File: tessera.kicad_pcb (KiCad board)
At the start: 4 copper layers, 0 parts

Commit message: feat(sch): preliminary Tessera Badge schematic
- Add sheets for LEDs, USB connector, MCU, NFC, power and STSAFE-A120.
- Drop the old placeholder sections.
- Bump the lib submodule and add IPN as a BOM column in the kibot
  outputs to reflect the DB-library parts now placed in the schematic.
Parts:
- added AE1: 13.56MHz_NFC_Antenna_N9, Antenna_NFC:NFC_40x30_N9_ST_ST25DV, F.Cu at (213.3, 60.8)
- added C1: 1uF 50V (X7R), Capacitor_SMD:C_0805_2012Metric, F.Cu at (200.0, 100.4)
- added C10: 10nF 16V (X7R), Capacitor_SMD:C_0402_1005Metric, F.Cu at (240.3, 41.2)
- added C11: UndefF, Capacitor_SMD:C_0402_1005Metric, F.Cu at (240.3, 43.2)
- added C12: 100nF 16V (X7R), Capacitor_SMD:C_0402_1005Metric, F.Cu at (240.3, 45.2)
- added C13: 100nF 16V (X7R), Capacitor_SMD:C_0402_1005Metric, F.Cu at (240.3, 47.2)
- added C14: UndefF, Capacitor_SMD:C_0402_1005Metric, F.Cu at (240.3, 49.1)
- added C15: UndefF, Capacitor_SMD:C_0402_1005Metric, F.Cu at (240.3, 51.1)
- added C16: UndefF, Capacitor_SMD:C_0402_1005Metric, F.Cu at (240.3, 53.1)
- added C17: UndefF, Capacitor_SMD:C_0402_1005Metric, F.Cu at (240.3, 55.0)
- added C18: 100nF 16V (X7R), Capacitor_SMD:C_0402_1005Metric, F.Cu at (249.1, 78.2)
- added C2: 1uF 50V (X7R), Capacitor_SMD:C_0805_2012Metric, F.Cu at (200.0, 103.4)
- added C3: 4.7uF 50V (X7R), Capacitor_SMD:C_1206_3216Metric, F.Cu at (205.1, 100.6)
- added C4: UndefF, Capacitor_SMD:C_0402_1005Metric, F.Cu at (189.3, 107.4)
- added C5: 10uF 50V (X7R), Capacitor_SMD:C_1210_3225Metric, F.Cu at (205.1, 104.4)
- added C6: 10uF 50V (X7R), Capacitor_SMD:C_1210_3225Metric, F.Cu at (222.6, 99.3)
- added C7: 100nF 16V (X7R), Capacitor_SMD:C_0402_1005Metric, F.Cu at (221.2, 106.6)
- added C8: 10uF 50V (X7R), Capacitor_SMD:C_1210_3225Metric, F.Cu at (222.6, 103.5)
- added C9: 100nF 16V (X7R), Capacitor_SMD:C_0402_1005Metric, F.Cu at (221.2, 108.6)
- added D1: APHHS1005SURCK, Leds:LED_0402_1005Metric, F.Cu at (254.8, 64.4)
- added D2: APHHS1005SURCK, Leds:LED_0402_1005Metric, F.Cu at (254.8, 66.4)
- added D3: APHHS1005SURCK, Leds:LED_0402_1005Metric, F.Cu at (254.8, 68.4)
- added J1: USB-C, Conn_USB:GCT_USB4520-03-1-A_REVA, F.Cu at (250.7, 47.3)
- added J2: 532610271, Conn_Molex:Molex_PicoBlade_53261-0271_1x02-1MP_P1.25mm_Horizontal, F.Cu at (197.1, 95.3)
- added J3: PinHeader_2x05, Conn_PinHeader:PinHeader_2x05_P1.27mm_Vertical_SMD_TRH, F.Cu at (214.0, 102.5)
- added L1: 2.2uH, Inductors:L_0806_2016Metric, F.Cu at (204.6, 92.5)
- added MECH1: FIDUCIAL, Mechanical:Fiducial_1mm_Mask2mm, F.Cu at (239.3, 92.8)
- added MECH2: FIDUCIAL, Mechanical:Fiducial_1mm_Mask2mm, F.Cu at (239.3, 96.4)
- added MECH3: FIDUCIAL, Mechanical:Fiducial_1mm_Mask2mm, F.Cu at (239.3, 99.9)
- added Q1: NTK3139P, Packages_TO_SOT:SOT-723, F.Cu at (189.6, 105.0)
- added Q2: NTK3134N, Packages_TO_SOT:SOT-723, F.Cu at (258.0, 64.8)
- added Q3: NTK3134N, Packages_TO_SOT:SOT-723, F.Cu at (258.0, 67.7)
- added R1: 10 kOhms, Resistor_SMD:R_0402_1005Metric, F.Cu at (246.6, 92.0)
- added R10: 510 kOhms, Resistor_SMD:R_0402_1005Metric, F.Cu at (249.5, 94.0)
- added R11: 510 kOhms, Resistor_SMD:R_0402_1005Metric, F.Cu at (249.5, 96.0)
- added R12: 0R ±5% 1/10W, Resistor_SMD:R_0603_1608Metric, F.Cu at (243.1, 99.8)
- added R13: 510 kOhms, Resistor_SMD:R_0402_1005Metric, F.Cu at (249.5, 98.0)
- added R14: 510 kOhms, Resistor_SMD:R_0402_1005Metric, F.Cu at (249.5, 100.0)
- added R15: 510 kOhms, Resistor_SMD:R_0402_1005Metric, F.Cu at (259.1, 41.3)
- added R16: 510 kOhms, Resistor_SMD:R_0402_1005Metric, F.Cu at (259.1, 43.2)
- added R17: 5.1 kOhms, Resistor_SMD:R_0402_1005Metric, F.Cu at (259.1, 45.2)
- added R18: 5.1 kOhms, Resistor_SMD:R_0402_1005Metric, F.Cu at (259.1, 47.2)
- added R19: 0R ±5% 1/10W, Resistor_SMD:R_0603_1608Metric, F.Cu at (189.8, 92.3)
- added R2: 10 kOhms, Resistor_SMD:R_0402_1005Metric, F.Cu at (246.6, 94.0)
- added R20: 0R ±5% 1/10W, Resistor_SMD:R_0603_1608Metric, F.Cu at (189.8, 94.8)
- added R21: 27 kOhms, Resistor_SMD:R_0402_1005Metric, F.Cu at (193.3, 99.9)
- added R22: 30 kOhms, Resistor_SMD:R_0402_1005Metric, F.Cu at (193.3, 101.9)
- added R23: 10 kOhms, Resistor_SMD:R_0402_1005Metric, F.Cu at (193.3, 103.9)
- added R24: 0R ±5% 1/10W, Resistor_SMD:R_0603_1608Metric, F.Cu at (189.8, 97.3)
- added R25: 0R ±5% 1/10W, Resistor_SMD:R_0603_1608Metric, F.Cu at (189.8, 99.8)
- added R26: 0R ±5% 1/10W, Resistor_SMD:R_0603_1608Metric, F.Cu at (189.8, 102.3)
- added R27: 100 kOhms, Resistor_SMD:R_0402_1005Metric, F.Cu at (193.3, 105.9)
- added R28: 52.3 kOhms, Resistor_SMD:R_0402_1005Metric, F.Cu at (193.3, 107.8)
- added R29: 0R ±5% 1/10W, Resistor_SMD:R_0603_1608Metric, F.Cu at (227.5, 98.4)
- added R3: 10 kOhms, Resistor_SMD:R_0402_1005Metric, F.Cu at (246.6, 96.0)
- added R30: 0R ±5% 1/10W, Resistor_SMD:R_0603_1608Metric, F.Cu at (227.5, 100.9)
- added R31: 330R ±1% 1/10W, Resistor_SMD:R_0603_1608Metric, F.Cu at (255.2, 56.7)
- added R32: 330R ±1% 1/10W, Resistor_SMD:R_0603_1608Metric, F.Cu at (255.2, 59.2)
- added R33: 330R ±1% 1/10W, Resistor_SMD:R_0603_1608Metric, F.Cu at (255.2, 61.7)
- added R34: 510 kOhms, Resistor_SMD:R_0402_1005Metric, F.Cu at (251.7, 56.4)
- added R35: 510 kOhms, Resistor_SMD:R_0402_1005Metric, F.Cu at (251.7, 58.4)
- added R36: 510 kOhms, Resistor_SMD:R_0402_1005Metric, F.Cu at (251.7, 60.4)
- added R37: 510 kOhms, Resistor_SMD:R_0402_1005Metric, F.Cu at (251.7, 62.4)
- added R38: 0R ±5% 1/10W, Resistor_SMD:R_0603_1608Metric, F.Cu at (189.8, 82.8)
- added R39: 0R ±5% 1/10W, Resistor_SMD:R_0603_1608Metric, F.Cu at (189.8, 85.3)
- added R4: 10 kOhms, Resistor_SMD:R_0402_1005Metric, F.Cu at (246.6, 98.0)
- added R40: 0R ±5% 1/10W, Resistor_SMD:R_0603_1608Metric, F.Cu at (189.8, 87.8)
- added R41: 0R ±5% 1/10W, Resistor_SMD:R_0603_1608Metric, F.Cu at (245.7, 76.4)
- added R42: 100 kOhms, Resistor_SMD:R_0402_1005Metric, F.Cu at (249.2, 76.2)
- added R43: 0R ±5% 1/10W, Resistor_SMD:R_0603_1608Metric, F.Cu at (245.7, 78.9)
- added R5: 0R ±5% 1/10W, Resistor_SMD:R_0603_1608Metric, F.Cu at (243.1, 92.3)
- added R6: 510 kOhms, Resistor_SMD:R_0402_1005Metric, F.Cu at (246.6, 100.0)
- added R7: 510 kOhms, Resistor_SMD:R_0402_1005Metric, F.Cu at (249.5, 92.0)
- added R8: 0R ±5% 1/10W, Resistor_SMD:R_0603_1608Metric, F.Cu at (243.1, 94.8)
- added R9: 0R ±5% 1/10W, Resistor_SMD:R_0603_1608Metric, F.Cu at (243.1, 97.3)
- added SW1: EVQP7A01P, Button_Switch:Panasonic_EVQP7K_EVQP7A, F.Cu at (247.0, 57.7)
- added SW2: EVQP7A01P, Button_Switch:Panasonic_EVQP7K_EVQP7A, F.Cu at (247.0, 62.8)
- added TP1: TP, Test:TestPoint_Pad_D1.0mm, F.Cu at (233.0, 92.6)
- added TP10: TP, Test:TestPoint_Pad_D1.0mm, F.Cu at (196.3, 106.5)
- added TP11: TP, Test:TestPoint_Pad_D1.0mm, F.Cu at (221.3, 92.6)
- added TP12: TP, Test:TestPoint_Pad_D1.0mm, F.Cu at (221.3, 95.6)
- added TP13: TP, Test:TestPoint_Pad_D1.0mm, F.Cu at (224.4, 92.6)
- added TP14: TP, Test:TestPoint_Pad_D1.0mm, F.Cu at (224.4, 95.6)
- added TP15: TP, Test:TestPoint_Pad_D1.0mm, F.Cu at (227.4, 92.6)
- added TP16: TP, Test:TestPoint_Pad_D1.0mm, F.Cu at (227.4, 95.6)
- added TP17: TP, Test:TestPoint_Pad_D1.0mm, F.Cu at (251.8, 64.9)
- added TP18: TP, Test:TestPoint_Pad_D1.0mm, F.Cu at (251.8, 68.0)
- added TP19: TP, Test:TestPoint_Pad_D1.0mm, F.Cu at (198.3, 83.0)
- added TP2: TP, Test:TestPoint_Pad_D1.0mm, F.Cu at (233.0, 95.6)
- added TP3: TP, Test:TestPoint_Pad_D1.0mm, F.Cu at (233.0, 98.7)
- added TP4: TP, Test:TestPoint_Pad_D1.0mm, F.Cu at (233.0, 101.7)
- added TP5: TP, Test:TestPoint_Pad_D1.0mm, F.Cu at (236.0, 92.6)
- added TP6: TP, Test:TestPoint_Pad_D1.0mm, F.Cu at (236.0, 95.6)
- added TP7: TP, Test:TestPoint_Pad_D1.0mm, F.Cu at (236.0, 98.7)
- added TP8: TP, Test:TestPoint_Pad_D1.0mm, F.Cu at (196.3, 100.4)
- added TP9: TP, Test:TestPoint_Pad_D1.0mm, F.Cu at (196.3, 103.5)
- added U1: USBLC6-2P6, Packages_TO_SOT:SOT-666, F.Cu at (245.7, 51.8)
- added U2: BQ25170J, Packages_SO_SON:WSON-8-1EP_2x2mm_P0.5mm_EP0.9x1.6mm, F.Cu at (204.4, 95.7)
- added U3: TPS62840DLCR, Packages_SO_SON:Texas_VSON-HR-8_1.5x2mm_P0.5mm, F.Cu at (199.9, 106.8)
- added U4: ISP1807-LR-RS, MCU:ISP1807-LR, F.Cu at (214.9, 95.9)
- added U5: D3V3XA4B10LP, Packages_DFN_QFN:Diodes_UDFN-10_1.0x2.5mm_P0.5mm, F.Cu at (227.0, 104.2)
- added U6: ST25DV64KC-JF6D3, Packages_DFN_QFN:ST_UFDFPN-12-1EP_3x3mm_P0.5mm_EP1.4x2.55mm, F.Cu at (194.5, 83.8)
- added U7: STSAFA120DFSPL05, Packages_DFN_QFN:ST_UFDFPN-8-1EP_2x3mm_P0.5mm_EP1.4x2.55mm, F.Cu at (246.3, 73.4)
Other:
- board outline added: 12.9 x 6.6 mm

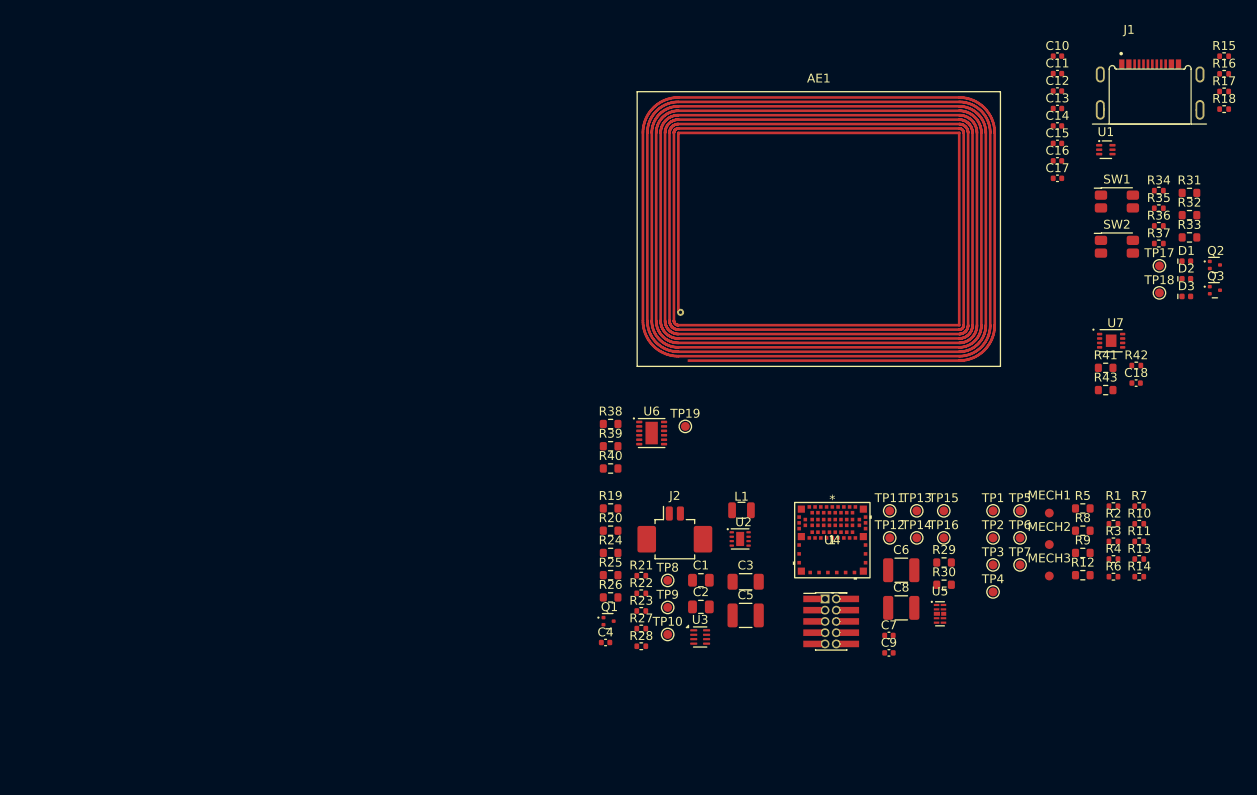
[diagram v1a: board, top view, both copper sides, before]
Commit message: fix(hardware): replace jumper/passive footprints with 0402 and refine schematics
- Replace 0-ohm jumper resistors with 0402 package equivalents
- Reduce package size on several capacitors
- Correct and simplify several schematic symbols (replaced with
  simplified equivalents where the original was overcomplicated)
- Bump lib submodule to the updated component library (renamed
  switch footprints, new Conn_01x02_MountingPin symbol, pad/pin
  numbering fixes, approved IPN assignments, Workart artwork library)
- Register Workart.pretty in fp-lib-table
- Mark J3 as DNP in mcu.kicad_sch
- Continue schematic wiring/placement (Leds.kicad_sch, tessera.kicad_sch)
  and PCB routing/placement (tessera.kicad_pcb)
- Add board outline source (Images/pcb_size.dxf, pcb_shape.FCStd) and
  silkscreen artwork sources (Logos/) for the Workart footprints
- Complete preliminary version of PCB
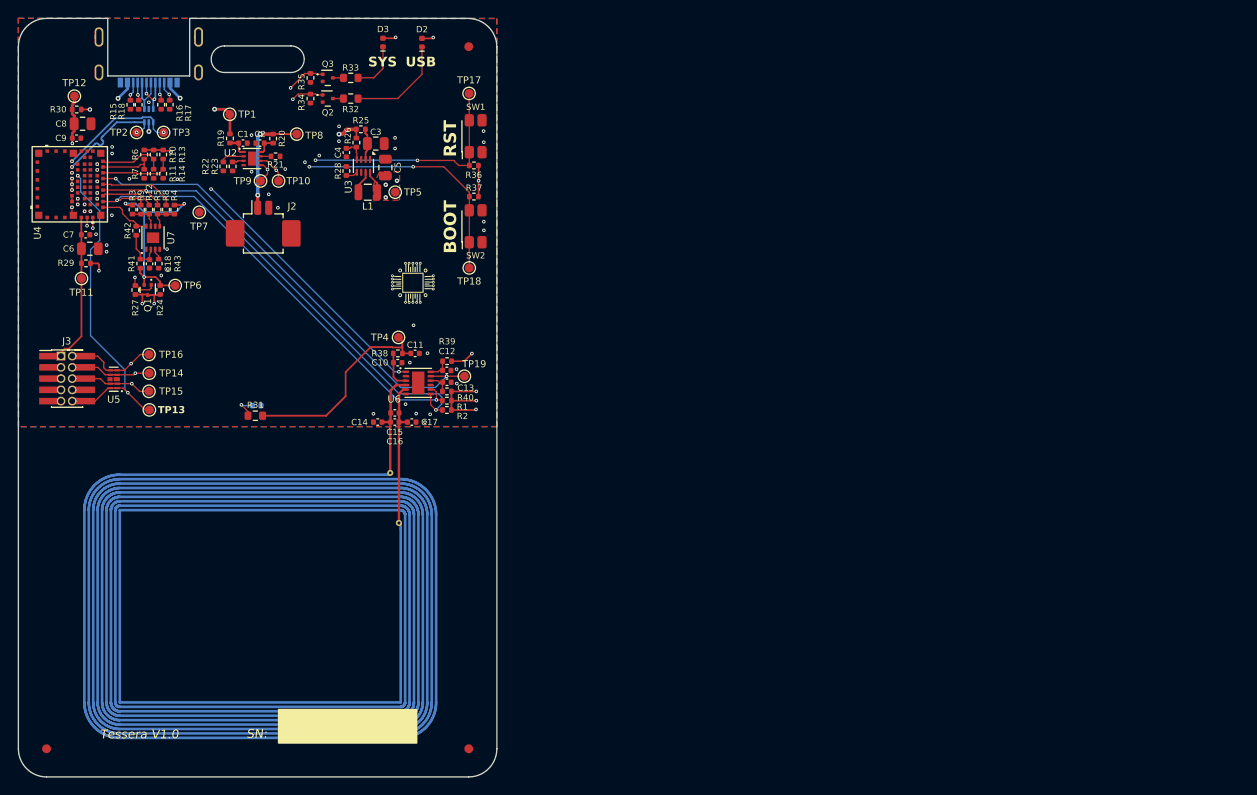
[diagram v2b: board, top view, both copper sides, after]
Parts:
- added G1: LOGO, Workart:logo_aps_4_5, F.Cu at (167.5, 66.8)
- added G2: LOGO, Workart:Name, B.Cu at (150.0, 56.4)
- added G3: LOGO, Workart:light_bulb_8_7_12, B.Cu at (150.0, 84.1)
- added G4: LOGO, Workart:linkedin_qr_with_linkedin_logo_inv, B.Cu at (149.8, 103.3)
- added G5: LOGO, Workart:bin_logo, B.Cu at (127.8, 75.0)
- AE1, D1, J1, U1: moved to B.Cu
- C1, C2: value 1uF 50V (X7R) -> 1uF 6.3V (X5R); footprint Capacitor_SMD:C_0805_2012Metric -> Capacitor_SMD:C_0402_1005Metric
- C3: value 4.7uF 50V (X7R) -> 4.7uF 6.3V (X7R); footprint Capacitor_SMD:C_1206_3216Metric -> Capacitor_SMD:C_0805_2012Metric
- C5, C6, C8: value 10uF 50V (X7R) -> 10uF 10V (X7R); footprint Capacitor_SMD:C_1210_3225Metric -> Capacitor_SMD:C_0805_2012Metric
- R12, R19, R20, R24, R25, R26, R29, R30, R38, R39, R40, R41, R43, R5, R8, R9: value 0R ±5% 1/10W -> 0R ±5% 1/16W; footprint Resistor_SMD:R_0603_1608Metric -> Resistor_SMD:R_0402_1005Metric
- SW1, SW2: footprint Button_Switch:Panasonic_EVQP7K_EVQP7A -> Button_Switch:Panasonic_switch_EVQP7K_EVQP7A
- moved R15 123.6 mm to (135.6, 46.7), turned to -90 degrees
- moved R18 122.5 mm to (136.6, 46.7), turned to -90 degrees
- moved R16 120.0 mm to (139.1, 46.7), turned to -90 degrees
- moved R6 119.3 mm to (137.2, 52.4), turned to -90 degrees
- moved R13 119.2 mm to (139.3, 52.4), turned to -90 degrees
- moved R14 119.2 mm to (139.3, 54.5), turned to -90 degrees
- moved R17 119.0 mm to (140.1, 46.7), turned to -90 degrees
- moved R10 118.8 mm to (138.3, 52.4), turned to -90 degrees
- moved R11 118.7 mm to (138.3, 54.5), turned to -90 degrees
- moved R7 118.4 mm to (137.2, 54.5), turned to -90 degrees
- moved R3 116.9 mm to (135.9, 58.6), turned to 90 degrees
- moved MECH1 116.3 mm to (126.2, 119.4)
- moved R42 113.9 mm to (136.3, 61.0), turned to 90 degrees
- moved J1 113.3 mm to (137.7, 39.1)
- moved R12 113.2 mm to (137.8, 58.6), turned to 90 degrees
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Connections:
- net Net-(J1-D+-PadA6) renamed /Project Architecture/USB/USB_D+
- net Net-(J1-D--PadA7) renamed /Project Architecture/USB/USB_D-
- C3 pad 1: VSYS -> Net-(U3-VIN)
- D1 pad 1: Net-(D1-K) -> GND
- D1 pad 2: VCC_EH -> Net-(D1-A)
- J1 pad S2: (no net) -> GND
- J1 pad S3: (no net) -> GND
- J1 pad S4: (no net) -> GND
- J2 pad MP: (no net) -> GND
- L1 pad 1: VCC -> Net-(U3-SW)
- L1 pad 2: /Project Architecture/power/VSense -> VCC
- R19 pad 1: /Project Architecture/power/VCH_IN -> VBUS
- R19 pad 2: VBUS -> /Project Architecture/power/VCH_IN
- R20 pad 1: VSYS -> /Project Architecture/power/VCH_OUT
- R20 pad 2: /Project Architecture/power/VCH_OUT -> VSYS
- R24 pad 1: VCC_SEC -> VCC
- R24 pad 2: VCC -> VCC_SEC
- R25 pad 1: Net-(U3-VIN) -> VSYS
- R25 pad 2: VSYS -> Net-(U3-VIN)
- R26 pad 2: Net-(U3-VIN) -> VSYS
- R29 pad 1: VCC_nRF -> VCC
- R29 pad 2: VCC -> VCC_nRF
- R30 pad 1: VBUS_nRF -> VBUS
- R30 pad 2: VBUS -> VBUS_nRF
- R31 pad 1: Net-(D1-K) -> VCC_EH
- R31 pad 2: GND -> Net-(D1-A)
- R36 pad 2: Net-(R36-Pad2) -> /Project Architecture/RST_PB
- R37 pad 2: Net-(R37-Pad2) -> /Project Architecture/USR_PB
- R38 pad 1: VCC_EH -> /Project Architecture/NFC/V_EH
- R38 pad 2: /Project Architecture/NFC/V_EH -> VCC_EH
- R41 pad 1: VCC_SEC -> Net-(U7-VCC)
- R41 pad 2: Net-(U7-VCC) -> VCC_SEC
- R42 pad 2: /Project Architecture/Secure element//RST -> /Project Architecture/SEC_RST
- R5 pad 1: /Project Architecture/Secure element/SDA -> /Project Architecture/SDA1
- R5 pad 2: /Project Architecture/SDA1 -> /Project Architecture/Secure element/SDA
- R9 pad 1: /Project Architecture/Secure element/SCL -> /Project Architecture/SCL1
- R9 pad 2: /Project Architecture/SCL1 -> /Project Architecture/Secure element/SCL
- U2 pad 9: (no net) -> GND
- U3 pad 7: VCC -> Net-(U3-SW)
- U3 pad 8: /Project Architecture/power/VSense -> VCC
- U4 pad 27: /Project Architecture/CHG_STAT -> /Project Architecture/SEC_PW_CTRL
- U4 pad 3: /Project Architecture/SDA1 -> unconnected-(U4-P0_12_TRACEDATA1-Pad3)
- U4 pad 32: /Project Architecture/SYS_LED -> /Project Architecture/SEC_RST
- U4 pad 33: /Project Architecture/HW_VER_2 -> unconnected-(U4-P0_07_TRACECLK-Pad33)
- U4 pad 34: /Project Architecture/USB_LED -> /Project Architecture/SCL1
- U4 pad 35: /Project Architecture/HW_VER_0 -> /Project Architecture/CHG_STAT
- U4 pad 36: /Project Architecture/SEC_PW_CTRL -> /Project Architecture/SCL2
- U4 pad 37: /Project Architecture/HW_VER_1 -> /Project Architecture/NFC_LOW_PWR
- U4 pad 38: /Project Architecture/SDA2 -> /Project Architecture/SDA1
- U4 pad 40: /Project Architecture/SCL2 -> /Project Architecture/SDA2
- U4 pad 41: unconnected-(U4-P0_25-Pad41) -> /Project Architecture/USR_PB
- U4 pad 44: /Project Architecture/NFC_LOW_PWR -> /Project Architecture/HW_VER_2
- U4 pad 45: unconnected-(U4-P0_19-Pad45) -> /Project Architecture/USB_LED
- U4 pad 46: unconnected-(U4-P0_29_AIN5-Pad46) -> /Project Architecture/HW_VER_0
- U4 pad 47: unconnected-(U4-P0_23-Pad47) -> /Project Architecture/SYS_LED
- U4 pad 48: /Project Architecture/USR_PB -> /Project Architecture/HW_VER_1
- U4 pad 5: /Project Architecture/SCL1 -> unconnected-(U4-P0_14-Pad5)
- U5 pad 10: /Project Architecture/MCU/SWDIO -> /Project Architecture/RST_PB
- U5 pad 6: (no net) -> /Project Architecture/MCU/SWDIO
- U7 pad 9: (no net) -> GND
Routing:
- net VCC: track 0.00 -> 163.7 mm, vias 0 -> 14
- net /Project Architecture/RST_PB: track 0.00 -> 90.3 mm, vias 0 -> 4
- net /Project Architecture/SDA1: track 0.00 -> 54.6 mm, vias 0 -> 2
- net /Project Architecture/SCL1: track 0.00 -> 53.1 mm, vias 0 -> 2
- net /Project Architecture/USR_PB: track 0.00 -> 53.0 mm, vias 0 -> 3
- net /Project Architecture/NFC_INT: track 0.00 -> 52.9 mm, vias 0 -> 2
- net /Project Architecture/NFC_LOW_PWR: track 0.00 -> 43.8 mm, vias 0 -> 3
- net /Project Architecture/MCU/SWDO: track 0.00 -> 30.7 mm, vias 0 -> 2
- net /Project Architecture/SYS_LED: track 0.00 -> 29.7 mm, vias 0 -> 2
- net /Project Architecture/USB_LED: track 0.00 -> 29.0 mm, vias 0 -> 2
- net /Project Architecture/MCU/SWDCLK: track 0.00 -> 27.8 mm, vias 0 -> 2
- net /Project Architecture/MCU/SWDIO: track 0.00 -> 27.8 mm, vias 0 -> 2
- net /Project Architecture/CHG_PG: track 0.00 -> 26.4 mm, vias 0 -> 2
- net VSYS: track 0.00 -> 24.7 mm, vias 0 -> 3
- net VCC_EH: track 0.00 -> 23.5 mm
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- added copper zone on B.Cu, net GND
- added copper zone on F.Cu, net GND
- added copper zone on In1.Cu, net GND
- added copper zone on In2.Cu, net GND
- added copper zone on In1.Cu, net VBUS
- added copper zone on F.Cu, net VCC
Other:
- board size 12.9 x 6.6 mm -> 54 x 85.6 mm
- board text added: "BOOT"
- board text added: "RST"
- board text added: "SN:"
- board text added: "SYS"
- board text added: "Tessera V1.0"
- board text added: "USB"
- board text added: "{ "ViaStitching": "0.2", "GND": { "HSpacing": "2", "VSpacing": "2", "Clearance": "0", "Randomize": false } }"
